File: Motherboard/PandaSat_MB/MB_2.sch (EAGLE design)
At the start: 88 parts, among them J1 503182-1852, J2 10118194-0001LF, J3 DCJ0303, Q10 IRLML5103, Q11 IRLML5103, Q13 IRLML2803, Q14 IRLML2803, Q15 IRLML2803, Q16 IRLML5103, Q17 2N5088, U1 MAX706R, U2 LTC4121-4.2, U3 LSM9DS1, U4 PE014006, U5 MAX4372TEUK+T, U6 RFM23BP, U7 TPS54226PWPRPWP14_2P31X2P46-L, U8 ATSAMD51, X1 BU-SMA-V

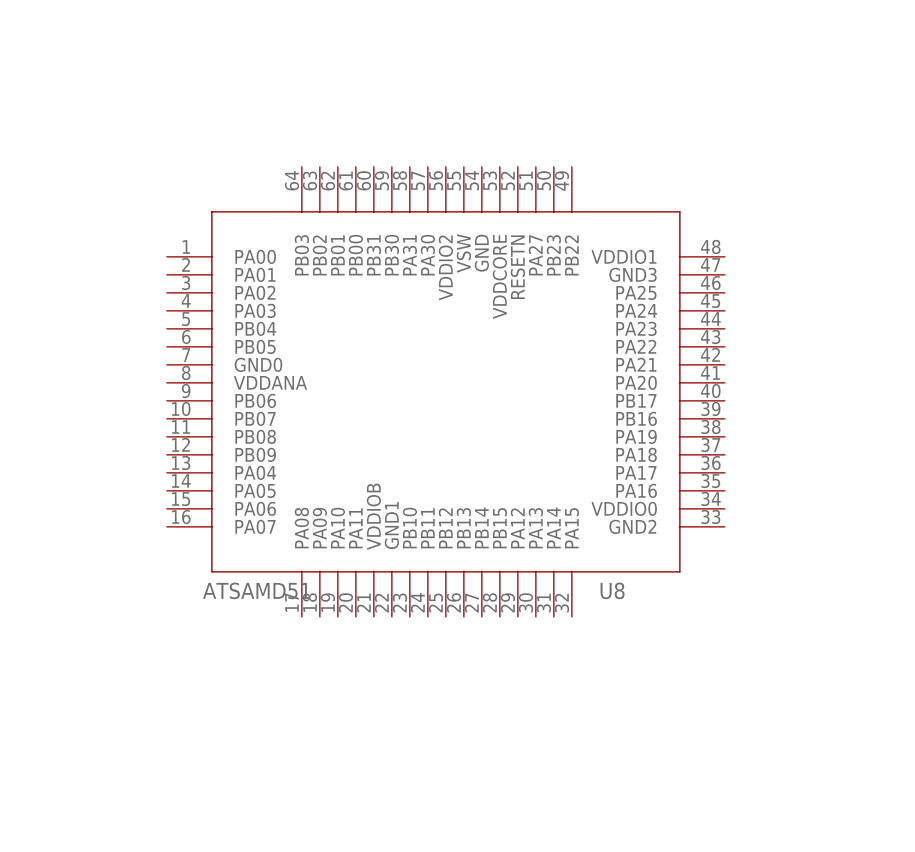
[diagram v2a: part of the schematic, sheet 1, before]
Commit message: 5V Power Circuit .. in progress
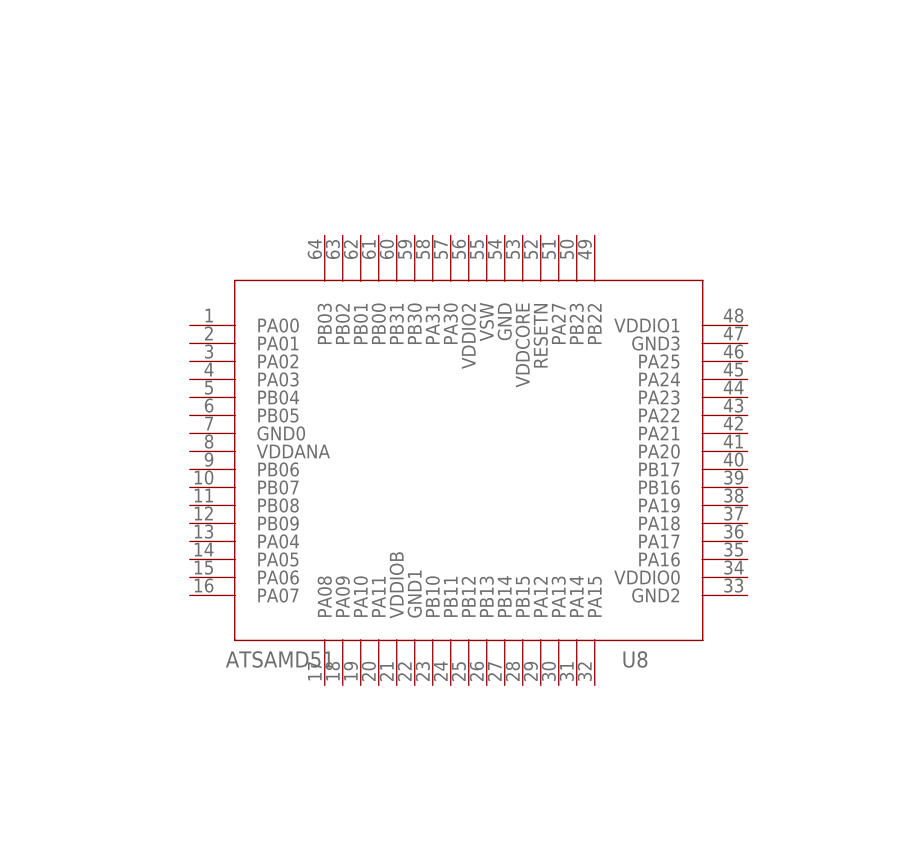
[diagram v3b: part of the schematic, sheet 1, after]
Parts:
- added JP6: JUMPER-PAD-3-2OF3_NC_BY_TRACE_SMALL, SparkFun-Passives:JUMPER-PAD-3-2OF3_NC_BY_TRACE_SMALL
- added R21: 1K34, resistor:R-US_R0603
- added R22: 100K, resistor:R-US_R0603
- added U9: OKL-T3-W12, pandasat:OKL-T3-W12
- U8: device atsamd5x:ATSAMD51 -> pandasat:ATSAMD51
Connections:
- net ENAB_GPS renamed ENAB_PAYLOAD
- net GPS_PWR_IN renamed PL_PWR_IN
- new net N$18: R21.1, U9.TRIM1
- new net N$19: JP6.1, U9.ON/OFF
- new net N$22: JP6.2, U9.VIN
- new net P_GOOD: R22.2, U9.PG
- net 3.3V: now also R22.1
- net 5V: now also U9.VOUT1
- net GND: now also R21.2, U9.GND0, U9.GND1
- net VBATT: now also JP6.3
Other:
- note added: "Payload Power"
- note removed: "GPS Power"
- moved on the sheet: U8
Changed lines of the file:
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@@
 <part name="X1" library="con-coax" library_urn="urn:adsk.eagle:library:133" deviceset="BU-SMA-V" device="" package3d_urn="urn:adsk.eagle:package:6211/1"/>
 <part name="GND20" library="supply1" library_urn="urn:adsk.eagle:library:371" deviceset="GND" device=""/>
-<part name="U8" library="atsamd5x" deviceset="ATSAMD51" device=""/>
 <part name="JP5" library="SparkFun-Passives" deviceset="JUMPER-PAD-3-2OF3_NC_BY_TRACE" device="_SMALL" value=""/>
 <part name="SUPPLY2" library="SparkFun-Aesthetics" deviceset="5V" device=""/>
@@
 <part name="R40" library="resistor" library_urn="urn:adsk.eagle:library:348" deviceset="R-US_" device="R0603" package3d_urn="urn:adsk.eagle:package:26057/1" value="2.1M"/>
 <part name="R41" library="resistor" library_urn="urn:adsk.eagle:library:348" deviceset="R-US_" device="R0603" package3d_urn="urn:adsk.eagle:package:26057/1" value="845K"/>
+<part name="U8" library="pandasat" deviceset="ATSAMD51" device=""/>
+<part name="U9" library="pandasat" deviceset="OKL-T3-W12" device=""/>
+<part name="GND22" library="supply1" library_urn="urn:adsk.eagle:library:371" deviceset="GND" device=""/>
+<part name="GND23" library="supply1" library_urn="urn:adsk.eagle:library:371" deviceset="GND" device=""/>
+<part name="R21" library="resistor" library_urn="urn:adsk.eagle:library:348" deviceset="R-US_" device="R0603" package3d_urn="urn:adsk.eagle:package:26057/1" value="1K34"/>
+<part name="GND24" library="supply1" library_urn="urn:adsk.eagle:library:371" deviceset="GND" device=""/>
+<part name="R22" library="resistor" library_urn="urn:adsk.eagle:library:348" deviceset="R-US_" device="R0603" package3d_urn="urn:adsk.eagle:package:26057/1" value="100K"/>
+<part name="P+4" library="SparkFun" deviceset="3.3V" device=""/>
+<part name="JP6" library="SparkFun-Passives" deviceset="JUMPER-PAD-3-2OF3_NC_BY_TRACE" device="_SMALL" value=""/>
 </parts>
 <sheets>
@@
 <attribute name="VALUE" x="76.2" y="15.24" size="1.778" layer="96" rot="MR0"/>
 </instance>
-<instance part="U8" gate="G$1" x="134.62" y="129.54" smashed="yes">
-<attribute name="NAME" x="185.62" y="90.54" size="1.778" layer="95"/>
-<attribute name="VALUE" x="141.62" y="90.54" size="1.778" layer="96"/>
-</instance>
 <instance part="JP5" gate="G$1" x="73.66" y="160.02" smashed="yes" rot="R90">
 <attribute name="NAME" x="73.279" y="162.56" size="1.778" layer="95" rot="R90"/>
@@
 <instance part="SUPPLY2" gate="G$1" x="22.86" y="38.1" smashed="yes">
 <attribute name="VALUE" x="21.844" y="41.656" size="1.778" layer="96"/>
+</instance>
+<instance part="U8" gate="G$1" x="137.16" y="121.92" smashed="yes">
+<attribute name="NAME" x="188.16" y="82.92" size="1.778" layer="95"/>
+<attribute name="VALUE" x="144.16" y="82.92" size="1.778" layer="96"/>
 </instance>
 </instances>
@@
 <text x="30.48" y="66.04" size="1.778" layer="97">Battery Current Sensor</text>
 <text x="154.94" y="7.62" size="3.175" layer="94">Matt Poole</text>
-<text x="193.04" y="76.2" size="2.54" layer="95">GPS Power</text>
+<text x="193.04" y="76.2" size="2.54" layer="95">Payload Power</text>
 <wire x1="147.32" y1="35.56" x2="147.32" y2="81.28" width="0.2032" layer="97" style="longdash"/>
 <wire x1="147.32" y1="81.28" x2="248.92" y2="81.28" width="0.2032" layer="97" style="longdash"/>
@@
 <attribute name="VALUE" x="40.64" y="162.56" size="1.778" layer="96" rot="R180"/>
 </instance>
+<instance part="U9" gate="G$1" x="55.88" y="109.22" smashed="yes">
+<attribute name="NAME" x="39.88" y="125.22" size="1.778" layer="95"/>
+<attribute name="VALUE" x="63.88" y="93.22" size="1.778" layer="96"/>
+</instance>
+<instance part="GND22" gate="1" x="20.32" y="109.22" smashed="yes">
+<attribute name="VALUE" x="17.78" y="106.68" size="1.778" layer="96"/>
+</instance>
+<instance part="GND23" gate="1" x="83.82" y="96.52" smashed="yes">
+<attribute name="VALUE" x="81.28" y="93.98" size="1.778" layer="96"/>
+</instance>
+<instance part="R21" gate="G$1" x="30.48" y="93.98" smashed="yes" rot="R270">
+<attribute name="NAME" x="31.9786" y="97.79" size="1.778" layer="95" rot="R270"/>
+<attribute name="VALUE" x="27.178" y="97.79" size="1.778" layer="96" rot="R270"/>
+</instance>
+<instance part="GND24" gate="1" x="35.56" y="86.36" smashed="yes">
+<attribute name="VALUE" x="33.02" y="83.82" size="1.778" layer="96"/>
+</instance>
+<instance part="R22" gate="G$1" x="81.28" y="116.84" smashed="yes" rot="R270">
+<attribute name="NAME" x="82.7786" y="120.65" size="1.778" layer="95" rot="R270"/>
+<attribute name="VALUE" x="77.978" y="120.65" size="1.778" layer="96" rot="R270"/>
+</instance>
+<instance part="P+4" gate="G$1" x="81.28" y="124.46" smashed="yes">
+<attribute name="VALUE" x="80.264" y="128.016" size="1.778" layer="96"/>
+</instance>
+<instance part="JP6" gate="G$1" x="20.32" y="121.92" smashed="yes" rot="MR90">
+<attribute name="NAME" x="20.701" y="124.46" size="1.778" layer="95" rot="MR90"/>
+<attribute name="VALUE" x="18.415" y="124.46" size="1.778" layer="96" rot="MR90"/>
+</instance>
 </instances>
 <busses>
@@
 <wire x1="35.56" y1="144.78" x2="43.18" y2="144.78" width="0.1524" layer="91"/>
 <junction x="43.18" y="144.78"/>
+</segment>
+<segment>
+<pinref part="U9" gate="G$1" pin="GND0"/>
+<pinref part="GND22" gate="1" pin="GND"/>
+<wire x1="35.88" y1="111.22" x2="35.88" y2="111.76" width="0.1524" layer="91"/>
+<wire x1="35.88" y1="111.76" x2="20.32" y2="111.76" width="0.1524" layer="91"/>
+</segment>
+<segment>
+<pinref part="U9" gate="G$1" pin="GND1"/>
+<pinref part="GND23" gate="1" pin="GND"/>
+<wire x1="75.88" y1="99.22" x2="75.88" y2="99.06" width="0.1524" layer="91"/>
+<wire x1="75.88" y1="99.06" x2="83.82" y2="99.06" width="0.1524" layer="91"/>
+</segment>
+<segment>
+<pinref part="GND24" gate="1" pin="GND"/>
+<pinref part="R21" gate="G$1" pin="2"/>
+<wire x1="35.56" y1="88.9" x2="30.48" y2="88.9" width="0.1524" layer="91"/>
 </segment>
 </net>
@@
 <label x="109.22" y="5.08" size="1.27" layer="95" rot="R180" xref="yes"/>
 </segment>
+<segment>
+<pinref part="P+4" gate="G$1" pin="3.3V"/>
+<pinref part="R22" gate="G$1" pin="1"/>
+<wire x1="81.28" y1="124.46" x2="81.28" y2="121.92" width="0.1524" layer="91"/>
+</segment>
 </net>
 <net name="I_BATT" class="0">
@@
 </segment>
 </net>
-<net name="ENAB_GPS" class="0">
+<net name="ENAB_PAYLOAD" class="0">
 <segment>
 <wire x1="180.34" y1="53.34" x2="177.8" y2="53.34" width="0.1524" layer="91"/>
@@
 <wire x1="43.18" y1="167.64" x2="35.56" y2="167.64" width="0.1524" layer="91"/>
 <junction x="43.18" y="167.64"/>
+</segment>
+<segment>
+<pinref part="JP6" gate="G$1" pin="3"/>
+<wire x1="15.24" y1="121.92" x2="10.16" y2="121.92" width="0.1524" layer="91"/>
+<label x="7.62" y="121.92" size="1.778" layer="95"/>
 </segment>
 </net>
@@
 </segment>
 </net>
-<net name="GPS_PWR_IN" class="0">
+<net name="PL_PWR_IN" class="0">
 <segment>
 <label x="241.3" y="48.26" size="1.27" layer="95" rot="R180" xref="yes"/>
@@
 </segment>
 </net>
+<net name="5V" class="0">
+<segment>
+<pinref part="U9" gate="G$1" pin="VOUT1"/>
+<wire x1="35.88" y1="107.22" x2="35.88" y2="106.68" width="0.1524" layer="91"/>
+<wire x1="35.88" y1="106.68" x2="33.02" y2="106.68" width="0.1524" layer="91"/>
+<label x="30.48" y="106.68" size="1.778" layer="95"/>
+</segment>
+</net>
+<net name="N$18" class="0">
+<segment>
+<pinref part="U9" gate="G$1" pin="TRIM1"/>
+<pinref part="R21" gate="G$1" pin="1"/>
+<wire x1="35.88" y1="99.22" x2="30.48" y2="99.22" width="0.1524" layer="91"/>
+<wire x1="30.48" y1="99.22" x2="30.48" y2="99.06" width="0.1524" layer="91"/>
+</segment>
+</net>
+<net name="P_GOOD" class="0">
+<segment>
+<pinref part="U9" gate="G$1" pin="PG"/>
+<wire x1="75.88" y1="111.22" x2="81.28" y2="111.22" width="0.1524" layer="91"/>
+<wire x1="81.28" y1="111.22" x2="81.28" y2="111.76" width="0.1524" layer="91"/>
+<label x="86.36" y="111.76" size="1.778" layer="95"/>
+<pinref part="R22" gate="G$1" pin="2"/>
+</segment>
+</net>
+<net name="N$19" class="0">
+<segment>
+<pinref part="JP6" gate="G$1" pin="1"/>
+<pinref part="U9" gate="G$1" pin="ON/OFF"/>
+<wire x1="25.4" y1="121.92" x2="25.4" y2="119.22" width="0.1524" layer="91"/>
+<wire x1="25.4" y1="119.22" x2="35.88" y2="119.22" width="0.1524" layer="91"/>
+</segment>
+</net>
+<net name="N$22" class="0">
+<segment>
+<pinref part="JP6" gate="G$1" pin="2"/>
+<pinref part="U9" gate="G$1" pin="VIN"/>
+<wire x1="20.32" y1="116.84" x2="20.32" y2="115.22" width="0.1524" layer="91"/>
+<wire x1="20.32" y1="115.22" x2="35.88" y2="115.22" width="0.1524" layer="91"/>
+</segment>
+</net>

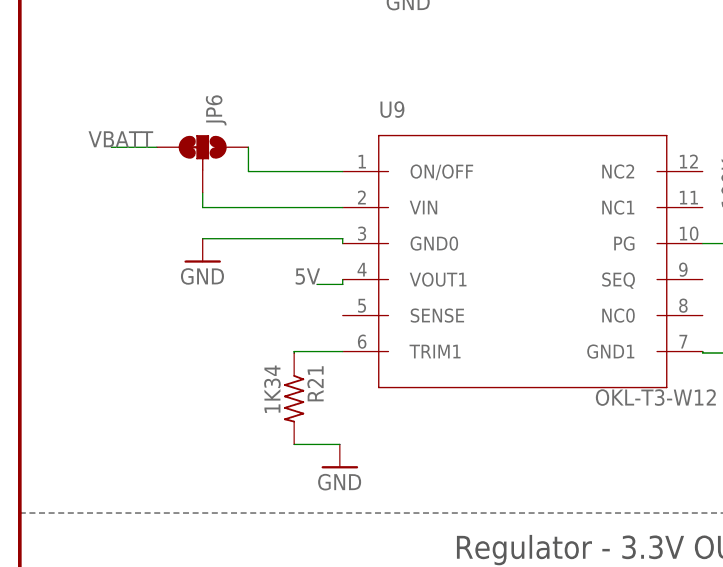
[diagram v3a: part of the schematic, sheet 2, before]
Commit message: Updated Watchdog timer & 5V reg
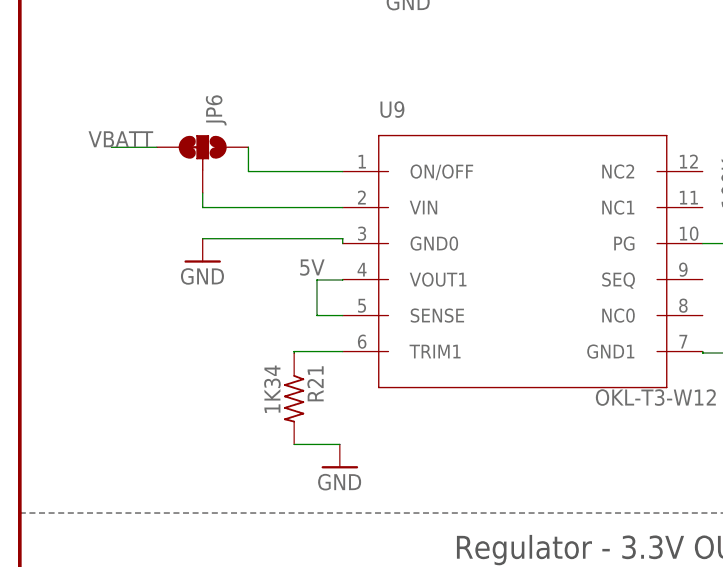
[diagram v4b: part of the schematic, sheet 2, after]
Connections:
- net 5V: now also U9.SENSE
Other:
- note added: "HopeRF RFM23B module at 5V"
- note removed: "HopeRF RFM23B module at 3.3V"
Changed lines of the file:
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@@
 <setting verticaltext="up"/>
 </settings>
-<grid distance="0.1" unitdist="inch" unit="inch" style="lines" multiple="1" display="no" altdistance="0.01" altunitdist="inch" altunit="inch"/>
+<grid distance="0.5" unitdist="mm" unit="mm" style="lines" multiple="1" display="no" altdistance="0.01" altunitdist="inch" altunit="inch"/>
 <layers>
 <layer number="1" name="Top" color="35" fill="1" visible="no" active="no"/>
@@
 <text x="33.02" y="137.16" size="2.54" layer="98" align="top-left">Decide on HOLD and !WP
 </text>
-<text x="15.24" y="53.34" size="2.54" layer="97" align="top-left">HopeRF RFM23B module at 3.3V</text>
+<text x="15.24" y="53.34" size="2.54" layer="97" align="top-left">HopeRF RFM23B module at 5V</text>
 </plain>
 <instances>
@@
 <segment>
 <pinref part="U9" gate="G$1" pin="VOUT1"/>
-<wire x1="35.88" y1="107.22" x2="35.88" y2="106.68" width="0.1524" layer="91"/>
-<wire x1="35.88" y1="106.68" x2="33.02" y2="106.68" width="0.1524" layer="91"/>
-<label x="30.48" y="106.68" size="1.778" layer="95"/>
-</segment>
-</net>
+<wire x1="35.88" y1="107.22" x2="35.88" y2="107.18" width="0.1524" layer="91"/>
+<wire x1="35.88" y1="107.18" x2="33.02" y2="107.18" width="0.1524" layer="91"/>
+<label x="30.98" y="107.68" size="1.778" layer="95"/>
+<pinref part="U9" gate="G$1" pin="SENSE"/>
+<wire x1="35.88" y1="103.22" x2="33.02" y2="103.22" width="0.1524" layer="91"/>
+<wire x1="33.02" y1="103.22" x2="33.02" y2="107.18" width="0.1524" layer="91"/>
+</segment>
+</net>
